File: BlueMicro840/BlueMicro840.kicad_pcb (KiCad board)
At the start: 2 copper layers, 20 x 32 mm, 36 parts, among them J2 Conn_01x02_Male, J3 DNP, Q1 SI2301CDS-T1-GE3, U1 AP2112K-3.3TRG1, U2 ProMicro, U3 AP2112K-3.3TRG1, U4 TP4054ST, U5 E73-2G4M08S1C-52840, Y2 32,768

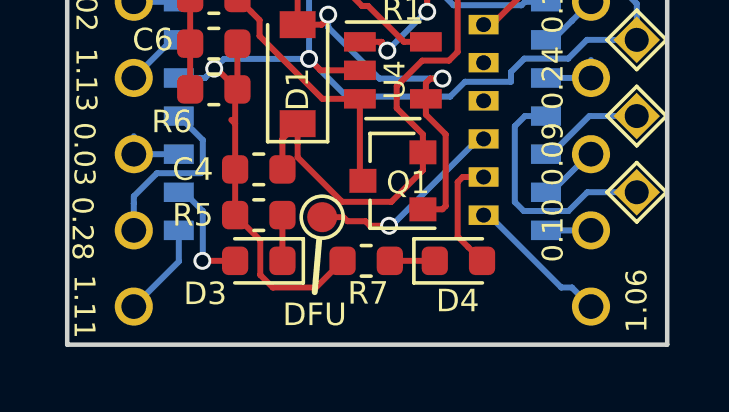
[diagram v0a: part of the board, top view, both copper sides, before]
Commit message: adding BOM to Docs
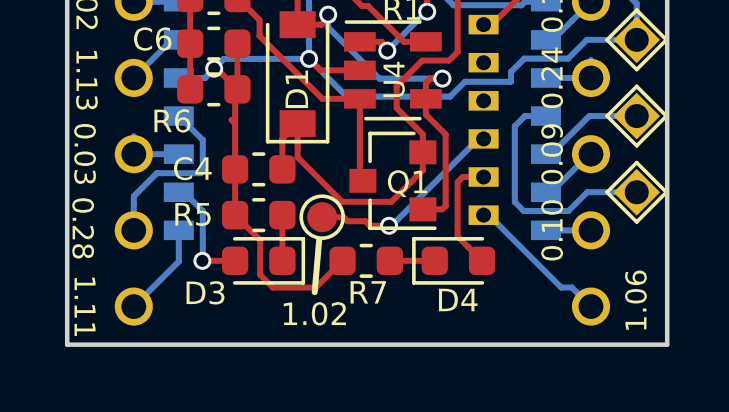
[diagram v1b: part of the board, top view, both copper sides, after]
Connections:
- net DFU renamed 1.02
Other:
- board text added: "1.02"
- board text removed: "DFU"

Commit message: fixed bluemacro840 schematic in docs
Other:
- board text added: "JLCJLCJLCJLC"
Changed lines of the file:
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@@
   (general
     (thickness 1.6)
-    (drawings 35)
+    (drawings 36)
     (tracks 561)
     (zones 0)
@@
   (module nrfmicro:E73-2G4M08S1C-52840 (layer B.Cu)
     (at 103.801533 123.722775 270)
-    (fp_text reference U5 (at 7.746775 0.000467) (layer B.SilkS)
+    (fp_text reference U5 (at 4.0732 0.0864) (layer B.SilkS)
       (effects (font (size 1 1) (thickness 0.15)) (justify mirror))
     )
@@
       (rotate (xyz 0 0 0))
     )
+  )
+  (gr_text JLCJLCJLCJLC (at 103.003933 133.739575 65) (layer B.SilkS)
+    (effects (font (size 0.75 0.75) (thickness 0.15)) (justify mirror))
   )
   (gr_line (start 102.361533 138.062775) (end 102.211533 139.812775) (layer F.SilkS) (width 0.2))
@@
   (segment (start 111.421533 125.851849) (end 110.245232 127.02815) (width 0.2) (layer F.Cu) (net 31))
   (segment (start 111.421533 125.052775) (end 111.421533 125.851849) (width 0.2) (layer F.Cu) (net 31) (status 10))
-  (via (at 104.690533 137.600375) (size 0.6) (drill 0.4) (layers F.Cu B.Cu) (net 45))
-  (segment (start 104.771933 137.600375) (end 104.690533 137.600375) (width 0.2) (layer B.Cu) (net 45))
-  (segment (start 107.842533 134.704775) (end 107.667533 134.704775) (width 0.2) (layer B.Cu) (net 45))
-  (segment (start 107.667533 134.704775) (end 104.771933 137.600375) (width 0.2) (layer B.Cu) (net 45))
-  (segment (start 104.055533 137.600375) (end 103.903133 137.447975) (width 0.2) (layer F.Cu) (net 45))
-  (segment (start 104.690533 137.600375) (end 104.055533 137.600375) (width 0.2) (layer F.Cu) (net 45))
-  (segment (start 103.303839 137.447975) (end 103.903133 137.447975) (width 0.2) (layer F.Cu) (net 45))
-  (segment (start 103.168639 137.312775) (end 103.303839 137.447975) (width 0.2) (layer F.Cu) (net 45))
-  (segment (start 102.461533 137.312775) (end 103.168639 137.312775) (width 0.2) (layer F.Cu) (net 45))
   (segment (start 111.422 132.075) (end 111.422 132.673) (width 0.2) (layer B.Cu) (net 32) (status 30))
   (segment (start 109.920533 132.672775) (end 111.421533 132.672775) (width 0.2) (layer B.Cu) (net 32) (status 30))
@@
   (segment (start 103.209533 120.558775) (end 102.906533 120.861775) (width 0.2) (layer F.Cu) (net 44))
   (via (at 102.658535 120.861775) (size 0.6) (drill 0.4) (layers F.Cu B.Cu) (net 44))
+  (via (at 104.690533 137.600375) (size 0.6) (drill 0.4) (layers F.Cu B.Cu) (net 45))
+  (segment (start 104.771933 137.600375) (end 104.690533 137.600375) (width 0.2) (layer B.Cu) (net 45))
+  (segment (start 107.842533 134.704775) (end 107.667533 134.704775) (width 0.2) (layer B.Cu) (net 45))
+  (segment (start 107.667533 134.704775) (end 104.771933 137.600375) (width 0.2) (layer B.Cu) (net 45))
+  (segment (start 104.055533 137.600375) (end 103.903133 137.447975) (width 0.2) (layer F.Cu) (net 45))
+  (segment (start 104.690533 137.600375) (end 104.055533 137.600375) (width 0.2) (layer F.Cu) (net 45))
+  (segment (start 103.303839 137.447975) (end 103.903133 137.447975) (width 0.2) (layer F.Cu) (net 45))
+  (segment (start 103.168639 137.312775) (end 103.303839 137.447975) (width 0.2) (layer F.Cu) (net 45))
+  (segment (start 102.461533 137.312775) (end 103.168639 137.312775) (width 0.2) (layer F.Cu) (net 45))
 )
